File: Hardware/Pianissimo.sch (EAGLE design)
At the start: 35 parts, among them Q1 5.8A/30V/35mΩ, Q2 600mA/40V

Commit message: initial revision with outline
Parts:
- removed C7, C8, C9: (no value), CalvEngIO-Passives:CAPACITOR0402
- removed Q1: 5.8A/30V/35mΩ, CalvEngIO-DiscreteSemi:NFET-AO3404A
- removed Q2: 600mA/40V, CalvEngIO-DiscreteSemi:NPN-MMBT2222AL
- removed R10, R15, R16, R17, R18, R9: (no value), CalvEngIO-Passives:RESISTOR0402
- removed R14: 10k, CalvEngIO-Passives:RESISTOR0402
- removed U$8: SPK-SR6438NWS-000, CalvEngIO-Electromechanical:SPK-SR6438NWS-000
- added C10, C18: 100n, CalvEngIO-Passives:CAPACITOR0402
- added C11, C12, C13, C14, C15, C20, C21, C22, C23, C24, C25: (no value), CalvEngIO-Passives:CAPACITOR0402
- added C26: (no value), CalvEngIO-Passives:CAPACITOR.POLARC-EEU-FM-A-220UF
- added C27: (no value), CalvEngIO-Passives:CAPACITOR0603
- added R19, R20, R34, R35: 10k, CalvEngIO-Passives:RESISTOR0402-SMALLER
- added R21, R36: 19k, CalvEngIO-Passives:RESISTOR0402-SMALLER
- added R22, R23, R24, R25, R37, R38, R39, R40, R47, R48: (no value), CalvEngIO-Passives:RESISTOR0402-SMALLER
- added R49: (no value), CalvEngIO-Passives:R-TRIMM5W
- added R50: (no value), CalvEngIO-Passives:RESISTOR0603
- added SPK1: (no value), CalvEngIO-Electromechanical:SPEAKER
- added U$16, U$19, U$24, U$27, U$29: 741.OP, CalvEngIO-AnalogIC:741.OP
- added U1: LM386N, SparkFun-IC-Amplifiers:LM386
- R1, R11, R12, R13, R2, R3, R4, R5, R6, R7: device CalvEngIO-Passives:RESISTOR0402 -> CalvEngIO-Passives:RESISTOR0402-SMALLER
- R8: value 10k -> (none); device CalvEngIO-Passives:RESISTOR0402 -> CalvEngIO-Passives:RESISTOR0402-SMALLER
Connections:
- removed net N$11: C9.2, R10.2, R9.1, U$7G$1.OUT
- removed net N$12: C9.1, R18.1, R9.2, U$7G$1.-IN
- removed net N$13: Q1.G, R11.2, R12.1
- removed net N$14: Q2.B, R10.1
- removed net N$15: Q2.C, U$8.-
- removed net N$16: R12.2, R13.2
- removed net N$17: C7.1, R16.1
- removed net N$18: C7.2, C8.1, R17.2, U$6G$1.-IN
- removed net N$19: R14.2, R15.1, U$6G$1.+IN
- removed net N$20: R18.2
- removed net N$21: C8.2, R17.1, U$6G$1.OUT
- new net N$22: R19.2, R21.1, R22.1, U$16G$1.OUT
- new net N$23: R19.1, R20.2, U$16G$1.+IN
- new net N$24: C10.2, R21.2, U$16G$1.-IN
- new net N$25: C12.1, R22.2, R23.1
- new net N$26: C13.1, R23.2, R24.1
- new net N$27: C14.1, R24.2, R25.1
- new net N$28: C15.1, R25.2, U$19G$1.+IN
- new net N$38: R34.2, R36.1, R37.1, U$24G$1.OUT
- new net N$39: R34.1, R35.2, U$24G$1.+IN
- new net N$40: C18.2, R36.2, U$24G$1.-IN
- new net N$41: C20.1, R37.2, R38.1
- new net N$42: C21.1, R38.2, R39.1
- new net N$43: C22.1, R39.2, R40.1
- new net N$44: C23.1, R40.2, U$27G$1.+IN
- new net N$50: C24.1, R47.1
- new net N$51: C1.2, C11.2, C24.2, C25.1, R48.2, U$29G$1.-IN
- new net N$54: R49.S, U1.+IN
- new net N$55: C25.2, R48.1, R49.E, U$29G$1.OUT
- new net N$56: C26.+, C27.1, U1.OUT
- new net N$57: C26.-, SPK1.+
- new net N$58: C27.2, R50.2
- new net NOTE_1: R11.2, U$27G$1.-IN, U$27G$1.OUT
- new net NOTE_2: R8.2, U$4G$1.-IN, U$4G$1.OUT
- new net NOTE_3: R47.2, U$19G$1.-IN, U$19G$1.OUT
- net GND: now also C10.1, C12.2, C13.2, C14.2, C15.2, C18.1, C20.2, C21.2, C22.2, C23.2, R12.2, R20.1, R35.1, R49.A, R50.1, SPK1.-, U1.-IN, U1.V-; no longer Q2.E, R11.1, R14.1, R8.1, U$7G$1.+IN
- net N$10: now also C1.1, R8.1; no longer R16.2, U$5G$1.-IN, U$5G$1.OUT
- net N$8: now also R12.1, R13.2, U$29G$1.+IN; no longer Q1.D, U$4G$1.-IN, U$4G$1.OUT
- net N$9: now also C11.1, R11.1; no longer Q1.S, R8.2, U$5G$1.+IN
- net V+: now also U$16G$2.V+, U$24G$2.V+, U1.V+; no longer C1.2, R15.2, U$8.+
- net V-: now also U$16G$2.V-, U$24G$2.V-; no longer C1.1
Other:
- note added: "Square Wave Oscillator"
- note added: "Square Wave to Sine Wave Converter using a 4-Pole Low-Pass Filter"
- note added: "Summing Amplifier and Active BandPass Filter"
- moved on the sheet: C1, C2, C3, C4, C5, C6, R1, R11, R12, R13, R2, R3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

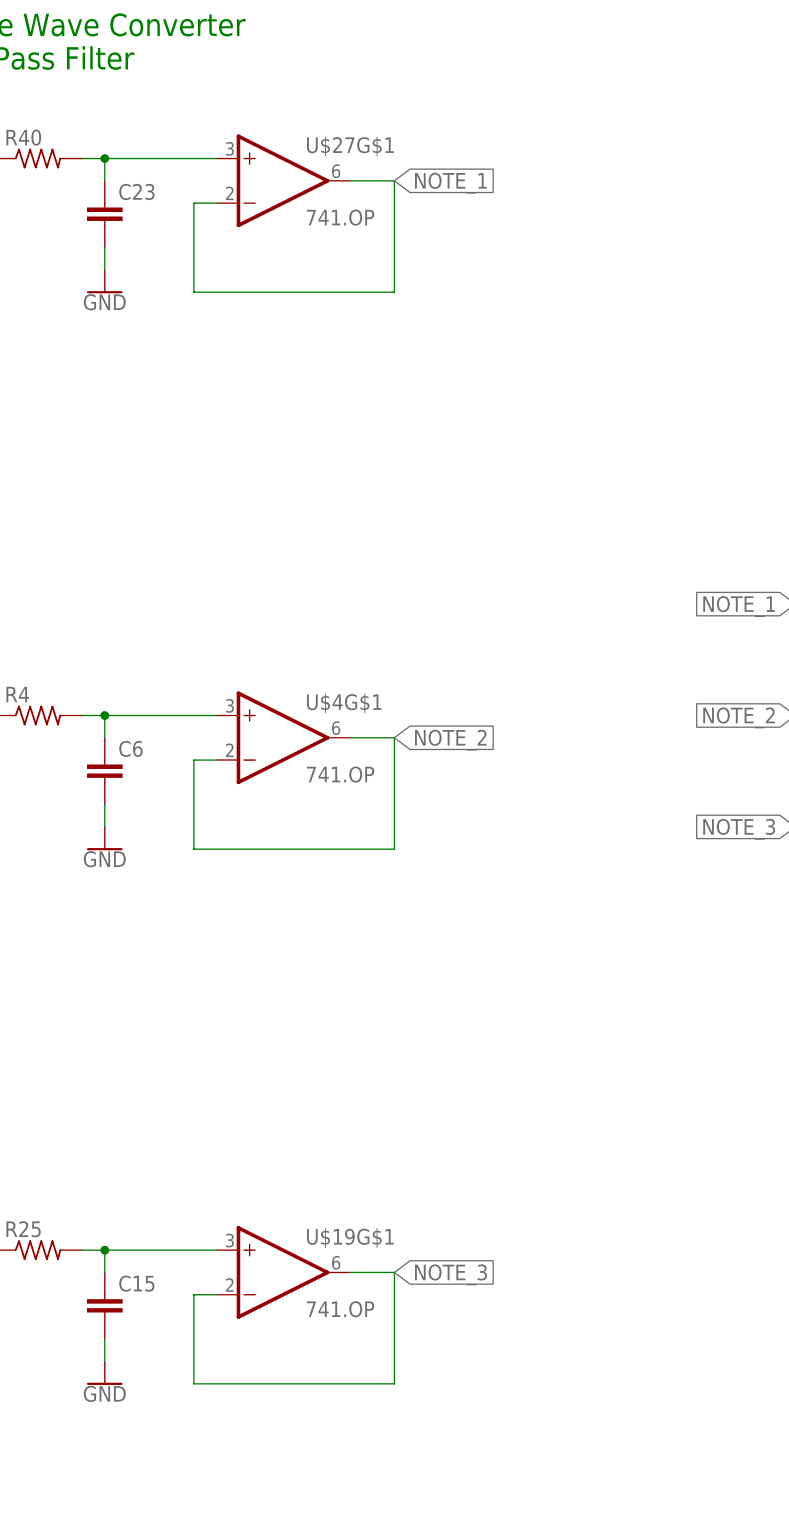
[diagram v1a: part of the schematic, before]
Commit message: added the pushbuttons
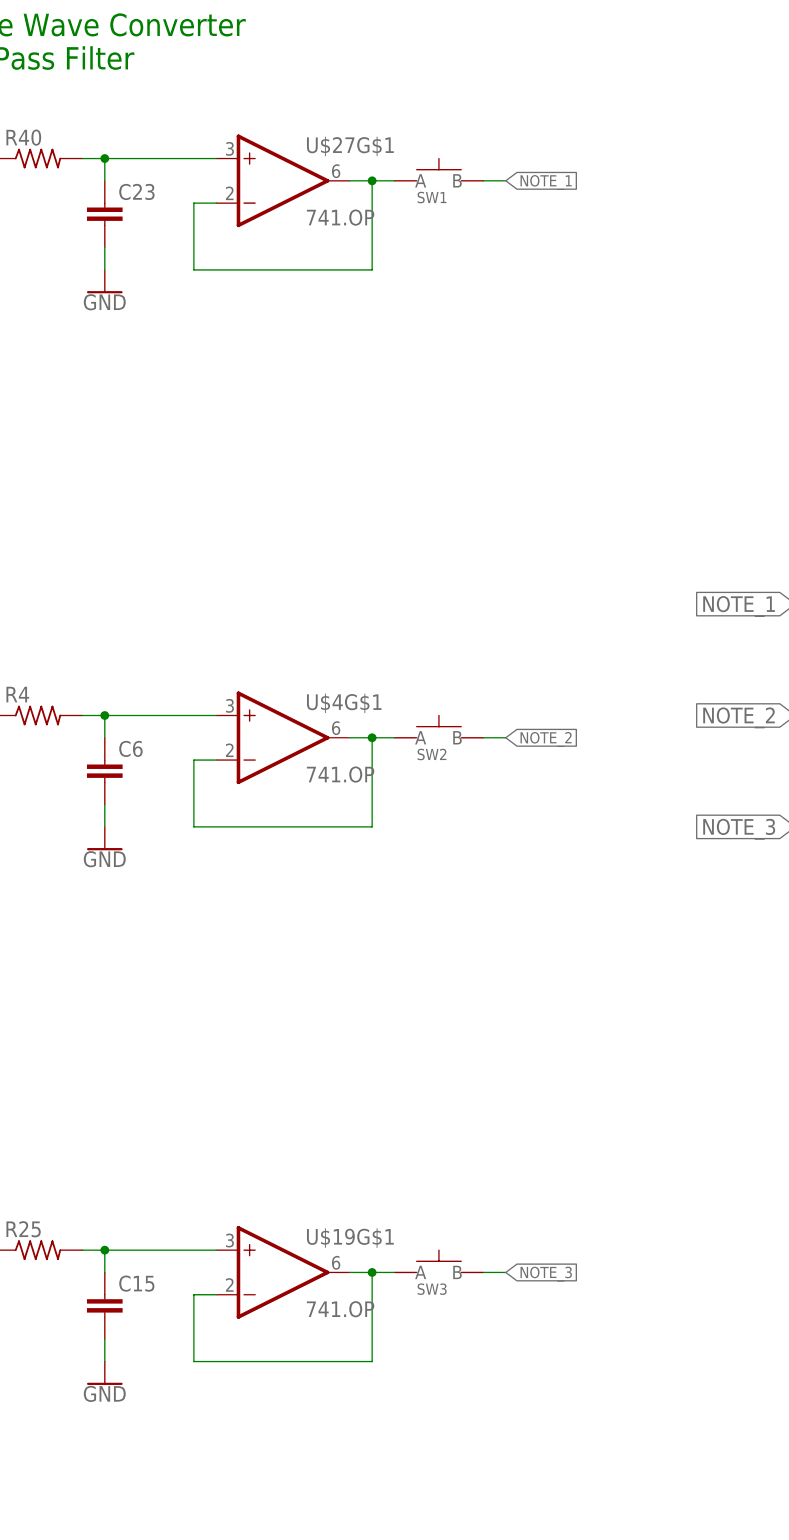
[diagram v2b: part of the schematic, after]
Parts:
- added SW1, SW2, SW3: (no value), CalvEngIO-Switches:SPST.KT11P4SM34LFS
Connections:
- new net N$11: SW1.A, U$27G$1.-IN, U$27G$1.OUT
- new net N$14: SW3.A, U$19G$1.-IN, U$19G$1.OUT
- new net N$16: SW2.A, U$4G$1.-IN, U$4G$1.OUT
- net NOTE_1: now also SW1.B; no longer U$27G$1.-IN, U$27G$1.OUT
- net NOTE_2: now also SW2.B; no longer U$4G$1.-IN, U$4G$1.OUT
- net NOTE_3: now also SW3.B; no longer U$19G$1.-IN, U$19G$1.OUT
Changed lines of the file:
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@@
 <part name="U$10" library="CalvEngIO-Symbols" deviceset="V+" device=""/>
 <part name="GND7" library="CalvEngIO-Symbols" deviceset="GND" device=""/>
+<part name="SW1" library="CalvEngIO-Switches" deviceset="SPST.KT11P4SM34LFS" device=""/>
+<part name="SW2" library="CalvEngIO-Switches" deviceset="SPST.KT11P4SM34LFS" device=""/>
+<part name="SW3" library="CalvEngIO-Switches" deviceset="SPST.KT11P4SM34LFS" device=""/>
 </parts>
 <sheets>
@@
 <attribute name="VALUE" x="312.42" y="20.066" size="1.778" layer="96" align="top-center"/>
 </instance>
+<instance part="SW1" gate="G$1" x="238.76" y="127" smashed="yes">
+<attribute name="NAME" x="236.22" y="124.46" size="1.27" layer="95"/>
+<attribute name="VALUE" x="236.22" y="121.92" size="1.27" layer="96"/>
+</instance>
+<instance part="SW2" gate="G$1" x="238.76" y="63.5" smashed="yes">
+<attribute name="NAME" x="236.22" y="60.96" size="1.27" layer="95"/>
+<attribute name="VALUE" x="236.22" y="58.42" size="1.27" layer="96"/>
+</instance>
+<instance part="SW3" gate="G$1" x="238.76" y="2.54" smashed="yes">
+<attribute name="NAME" x="236.22" y="0" size="1.27" layer="95"/>
+<attribute name="VALUE" x="236.22" y="-2.54" size="1.27" layer="96"/>
+</instance>
 </instances>
 <busses>
@@
 <net name="NOTE_2" class="0">
 <segment>
-<pinref part="U$4" gate="G$1" pin="-IN"/>
-<wire x1="213.36" y1="60.96" x2="210.82" y2="60.96" width="0.1524" layer="91"/>
-<wire x1="210.82" y1="60.96" x2="210.82" y2="50.8" width="0.1524" layer="91"/>
-<wire x1="210.82" y1="50.8" x2="233.68" y2="50.8" width="0.1524" layer="91"/>
-<wire x1="233.68" y1="50.8" x2="233.68" y2="63.5" width="0.1524" layer="91"/>
-<pinref part="U$4" gate="G$1" pin="OUT"/>
-<wire x1="233.68" y1="63.5" x2="228.6" y2="63.5" width="0.1524" layer="91"/>
-<label x="233.68" y="63.5" size="1.778" layer="95" xref="yes"/>
-</segment>
-<segment>
 <pinref part="R8" gate="G$1" pin="2"/>
 <wire x1="284.48" y1="66.04" x2="279.4" y2="66.04" width="0.1524" layer="91"/>
 <label x="279.4" y="66.04" size="1.778" layer="95" rot="R180" xref="yes"/>
+</segment>
+<segment>
+<pinref part="SW2" gate="G$1" pin="B"/>
+<wire x1="243.84" y1="63.5" x2="246.38" y2="63.5" width="0.1524" layer="91"/>
+<label x="246.38" y="63.5" size="1.27" layer="95" xref="yes"/>
 </segment>
 </net>
@@
 <net name="NOTE_3" class="0">
 <segment>
-<pinref part="U$19" gate="G$1" pin="-IN"/>
-<wire x1="213.36" y1="0" x2="210.82" y2="0" width="0.1524" layer="91"/>
-<wire x1="210.82" y1="0" x2="210.82" y2="-10.16" width="0.1524" layer="91"/>
-<wire x1="210.82" y1="-10.16" x2="233.68" y2="-10.16" width="0.1524" layer="91"/>
-<wire x1="233.68" y1="-10.16" x2="233.68" y2="2.54" width="0.1524" layer="91"/>
-<pinref part="U$19" gate="G$1" pin="OUT"/>
-<wire x1="233.68" y1="2.54" x2="228.6" y2="2.54" width="0.1524" layer="91"/>
-<label x="233.68" y="2.54" size="1.778" layer="95" xref="yes"/>
-</segment>
-<segment>
 <pinref part="R47" gate="G$1" pin="2"/>
 <wire x1="284.48" y1="53.34" x2="279.4" y2="53.34" width="0.1524" layer="91"/>
 <label x="279.4" y="53.34" size="1.778" layer="95" rot="R180" xref="yes"/>
+</segment>
+<segment>
+<pinref part="SW3" gate="G$1" pin="B"/>
+<wire x1="243.84" y1="2.54" x2="246.38" y2="2.54" width="0.1524" layer="91"/>
+<label x="246.38" y="2.54" size="1.27" layer="95" xref="yes"/>
 </segment>
 </net>
@@
 <net name="NOTE_1" class="0">
 <segment>
-<pinref part="U$27" gate="G$1" pin="-IN"/>
-<wire x1="213.36" y1="124.46" x2="210.82" y2="124.46" width="0.1524" layer="91"/>
-<wire x1="210.82" y1="124.46" x2="210.82" y2="114.3" width="0.1524" layer="91"/>
-<wire x1="210.82" y1="114.3" x2="233.68" y2="114.3" width="0.1524" layer="91"/>
-<wire x1="233.68" y1="114.3" x2="233.68" y2="127" width="0.1524" layer="91"/>
-<pinref part="U$27" gate="G$1" pin="OUT"/>
-<wire x1="233.68" y1="127" x2="228.6" y2="127" width="0.1524" layer="91"/>
-<label x="233.68" y="127" size="1.778" layer="95" xref="yes"/>
-</segment>
-<segment>
 <pinref part="R11" gate="G$1" pin="2"/>
 <wire x1="284.48" y1="78.74" x2="279.4" y2="78.74" width="0.1524" layer="91"/>
 <label x="279.4" y="78.74" size="1.778" layer="95" rot="R180" xref="yes"/>
+</segment>
+<segment>
+<pinref part="SW1" gate="G$1" pin="B"/>
+<wire x1="243.84" y1="127" x2="246.38" y2="127" width="0.1524" layer="91"/>
+<label x="246.38" y="127" size="1.27" layer="95" xref="yes"/>
 </segment>
 </net>
@@
 </segment>
 </net>
+<net name="N$11" class="0">
+<segment>
+<pinref part="U$27" gate="G$1" pin="OUT"/>
+<pinref part="SW1" gate="G$1" pin="A"/>
+<wire x1="233.68" y1="127" x2="231.14" y2="127" width="0.1524" layer="91"/>
+<pinref part="U$27" gate="G$1" pin="-IN"/>
+<wire x1="231.14" y1="127" x2="228.6" y2="127" width="0.1524" layer="91"/>
+<wire x1="213.36" y1="124.46" x2="210.82" y2="124.46" width="0.1524" layer="91"/>
+<wire x1="210.82" y1="124.46" x2="210.82" y2="116.84" width="0.1524" layer="91"/>
+<wire x1="210.82" y1="116.84" x2="231.14" y2="116.84" width="0.1524" layer="91"/>
+<wire x1="231.14" y1="116.84" x2="231.14" y2="127" width="0.1524" layer="91"/>
+<junction x="231.14" y="127"/>
+</segment>
+</net>
+<net name="N$14" class="0">
+<segment>
+<pinref part="U$19" gate="G$1" pin="OUT"/>
+<pinref part="SW3" gate="G$1" pin="A"/>
+<wire x1="233.68" y1="2.54" x2="231.14" y2="2.54" width="0.1524" layer="91"/>
+<pinref part="U$19" gate="G$1" pin="-IN"/>
+<wire x1="231.14" y1="2.54" x2="228.6" y2="2.54" width="0.1524" layer="91"/>
+<wire x1="213.36" y1="0" x2="210.82" y2="0" width="0.1524" layer="91"/>
+<wire x1="210.82" y1="0" x2="210.82" y2="-7.62" width="0.1524" layer="91"/>
+<wire x1="210.82" y1="-7.62" x2="231.14" y2="-7.62" width="0.1524" layer="91"/>
+<wire x1="231.14" y1="-7.62" x2="231.14" y2="2.54" width="0.1524" layer="91"/>
+<junction x="231.14" y="2.54"/>
+</segment>
+</net>
+<net name="N$16" class="0">
+<segment>
+<pinref part="U$4" gate="G$1" pin="-IN"/>
+<wire x1="213.36" y1="60.96" x2="210.82" y2="60.96" width="0.1524" layer="91"/>
+<wire x1="210.82" y1="60.96" x2="210.82" y2="53.34" width="0.1524" layer="91"/>
+<wire x1="210.82" y1="53.34" x2="231.14" y2="53.34" width="0.1524" layer="91"/>
+<wire x1="231.14" y1="53.34" x2="231.14" y2="63.5" width="0.1524" layer="91"/>
+<pinref part="U$4" gate="G$1" pin="OUT"/>
+<pinref part="SW2" gate="G$1" pin="A"/>
+<wire x1="233.68" y1="63.5" x2="231.14" y2="63.5" width="0.1524" layer="91"/>
+<wire x1="231.14" y1="63.5" x2="228.6" y2="63.5" width="0.1524" layer="91"/>
+<junction x="231.14" y="63.5"/>
+</segment>
+</net>

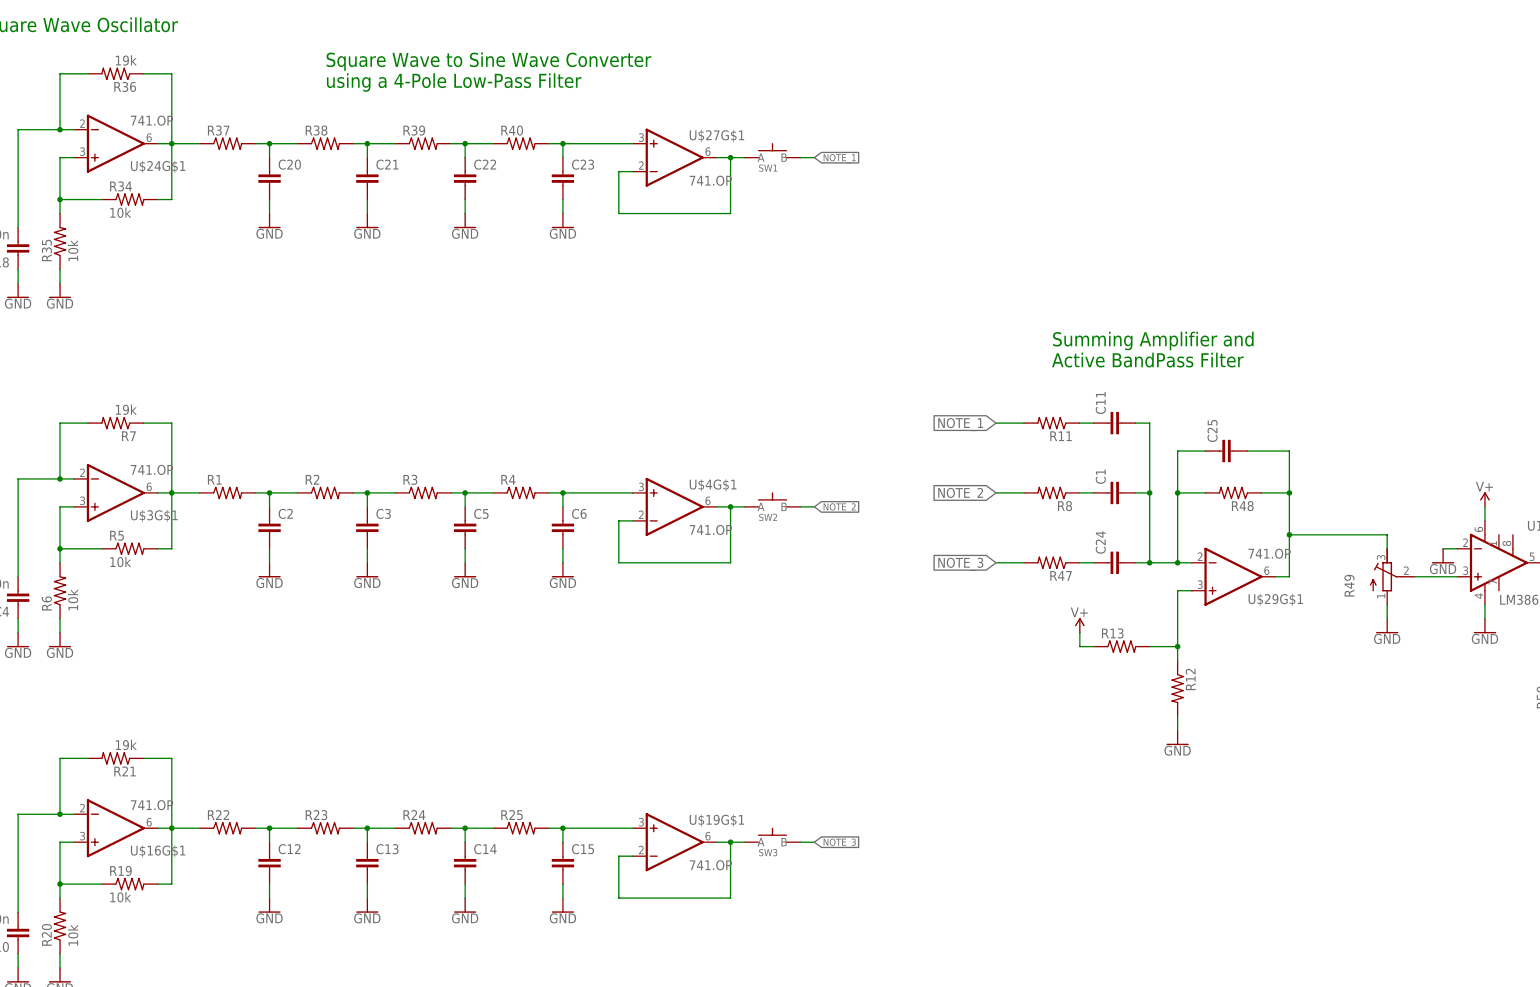
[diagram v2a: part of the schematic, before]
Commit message: added values corresponding to Mary Had a Little Lamb
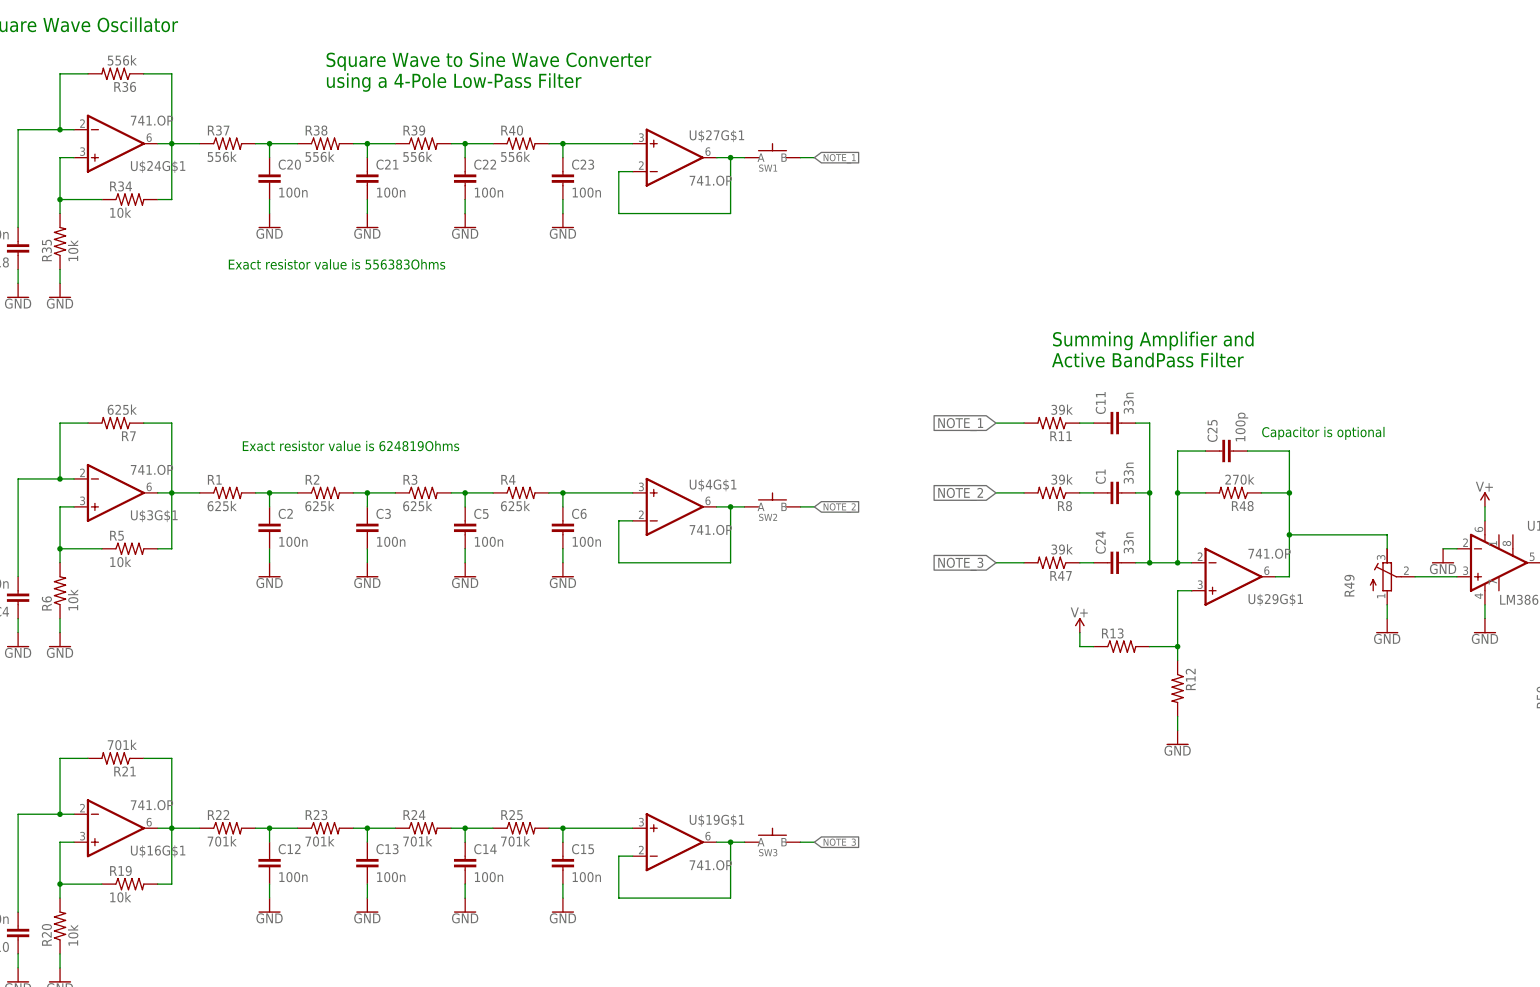
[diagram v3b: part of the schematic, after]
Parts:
- C1, C11, C24: value (none) -> 33n
- C12, C13, C14, C15, C2, C20, C21, C22, C23, C3, C5, C6: value (none) -> 100n
- C25: value (none) -> 100p
- R1, R2, R3, R4: value (none) -> 625k
- R11, R47, R8: value (none) -> 39k
- R21: value 19k -> 701k
- R22, R23, R24, R25: value (none) -> 701k
- R36: value 19k -> 556k
- R37, R38, R39, R40: value (none) -> 556k
- R48: value (none) -> 270k
- R7: value 19k -> 625k
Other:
- note added: "Capacitor is optional"
- note added: "Exact resistor value is 556383Ohms"
- note added: "Exact resistor value is 624819Ohms"
